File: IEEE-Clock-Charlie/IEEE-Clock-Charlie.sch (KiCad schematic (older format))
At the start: 4 parts

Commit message: First rev ordered OSHPARK
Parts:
- added L1: IEE_LOGO, IEEE-Clock-Charlie:IEEE_LOGO, symbol ADA_ROTARY:IEE_LOGO
- added R1: R, Resistor_SMD:R_0603_1608Metric, symbol Device:R
- added S1: PEC11R-4215F-S0024, IEEE-Clock-Charlie:RotaryEncoder_Alps_EC11E_Vertical_H20mm, symbol ADA_ROTARY:PEC11R-4215F-S0024
- added U4: ADA_DS3231, Connector_PinHeader_2.54mm:PinHeader_1x08_P2.54mm_Vertical, symbol ADA_DS3231:ADA_DS3231
- U1, U2, U3: renamed from U?; footprint MODULE -> IEEE-Clock-Charlie:DIP-26_1000_ELL
- gave numbers to parts that had none: 1
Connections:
- wire segments 55 -> 86
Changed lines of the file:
@@
 $EndDescr
 $Comp
-L MCU_Module:Arduino_Nano_v3.x A?
+L MCU_Module:Arduino_Nano_v3.x A1
 U 1 1 5E1FF514
 P 5550 5700
-F 0 "A?" H 5550 4611 50  0000 C CNN
+F 0 "A1" H 5550 4611 50  0000 C CNN
 F 1 "Arduino_Nano_v3.x" H 5550 4520 50  0000 C CNN
 F 2 "Module:Arduino_Nano" H 5700 4750 50  0001 L CNN
@@
 $EndComp
 $Comp
-L ADA_CHARLIE:ADA_CHARLIE U?
+L ADA_CHARLIE:ADA_CHARLIE U2
 U 1 1 5E23BD19
 P 5600 2850
-F 0 "U?" H 5600 3815 50  0000 C CNN
+F 0 "U2" H 5600 3815 50  0000 C CNN
 F 1 "ADA_CHARLIE" H 5600 3724 50  0000 C CNN
-F 2 "MODULE" H 5600 2850 50  0001 C CNN
+F 2 "IEEE-Clock-Charlie:DIP-26_1000_ELL" H 5600 2850 50  0001 C CNN
 F 3 "DOCUMENTATION" H 5600 2850 50  0001 C CNN
 	1    5600 2850
@@
 $EndComp
 $Comp
-L ADA_CHARLIE:ADA_CHARLIE U?
+L ADA_CHARLIE:ADA_CHARLIE U3
 U 1 1 5E23D5CF
 P 8400 2800
-F 0 "U?" H 8400 3765 50  0000 C CNN
+F 0 "U3" H 8400 3765 50  0000 C CNN
 F 1 "ADA_CHARLIE" H 8400 3674 50  0000 C CNN
-F 2 "MODULE" H 8400 2800 50  0001 C CNN
+F 2 "IEEE-Clock-Charlie:DIP-26_1000_ELL" H 8400 2800 50  0001 C CNN
 F 3 "DOCUMENTATION" H 8400 2800 50  0001 C CNN
 	1    8400 2800
@@
 	5750 4350 6350 4350
 $Comp
-L power:GND #PWR?
+L power:GND #PWR0101
 U 1 1 5E24D885
 P 4400 4550
-F 0 "#PWR?" H 4400 4300 50  0001 C CNN
+F 0 "#PWR0101" H 4400 4300 50  0001 C CNN
 F 1 "GND" H 4405 4377 50  0000 C CNN
 F 2 "" H 4400 4550 50  0001 C CNN
@@
 $EndComp
 $Comp
-L power:GND #PWR?
+L power:GND #PWR0102
 U 1 1 5E24E445
 P 5600 7150
-F 0 "#PWR?" H 5600 6900 50  0001 C CNN
+F 0 "#PWR0102" H 5600 6900 50  0001 C CNN
 F 1 "GND" H 5605 6977 50  0000 C CNN
 F 2 "" H 5600 7150 50  0001 C CNN
@@
 	4300 4350 5750 4350
 $Comp
-L ADA_CHARLIE:ADA_CHARLIE U?
+L ADA_CHARLIE:ADA_CHARLIE U1
 U 1 1 5E23A680
 P 3550 2800
-F 0 "U?" H 3550 3765 50  0000 C CNN
+F 0 "U1" H 3550 3765 50  0000 C CNN
 F 1 "ADA_CHARLIE" H 3550 3674 50  0000 C CNN
-F 2 "MODULE" H 3550 2800 50  0001 C CNN
+F 2 "IEEE-Clock-Charlie:DIP-26_1000_ELL" H 3550 2800 50  0001 C CNN
 F 3 "DOCUMENTATION" H 3550 2800 50  0001 C CNN
 	1    3550 2800
@@
 	2600 2300 2600 4050
 Wire Wire Line
-	2600 4050 4600 4050
+	2600 4050 3700 4050
 Connection ~ 4600 4050
+$Comp
+L ADA_DS3231:ADA_DS3231 U4
+U 1 1 5E30AA37
+P 2450 5450
+F 0 "U4" H 2292 6165 50  0000 C CNN
+F 1 "ADA_DS3231" H 2292 6074 50  0000 C CNN
+F 2 "Connector_PinHeader_2.54mm:PinHeader_1x08_P2.54mm_Vertical" H 2450 5450 50  0001 C CNN
+F 3 "DOCUMENTATION" H 2450 5450 50  0001 C CNN
+	1    2450 5450
+	-1   0    0    -1
+$EndComp
+Wire Wire Line
+	3200 5300 3600 5300
+Wire Wire Line
+	3600 5300 3600 3950
+Wire Wire Line
+	3600 3950 4500 3950
+Connection ~ 4500 3950
+Wire Wire Line
+	3200 5400 3700 5400
+Wire Wire Line
+	3700 5400 3700 4050
+Connection ~ 3700 4050
+Wire Wire Line
+	3700 4050 4600 4050
+Wire Wire Line
+	3200 5200 3300 5200
+Wire Wire Line
+	3300 5200 3300 4250
+Wire Wire Line
+	3300 4250 4400 4250
+Wire Wire Line
+	3200 5100 3200 4350
+Wire Wire Line
+	3200 4350 4300 4350
+Connection ~ 4300 4350
+Wire Wire Line
+	5050 5300 4050 5300
+Wire Wire Line
+	4050 5600 3200 5600
+$Comp
+L Device:R R1
+U 1 1 5E31C3B9
+P 4050 5450
+F 0 "R1" H 4120 5496 50  0000 L CNN
+F 1 "R" H 4120 5405 50  0000 L CNN
+F 2 "Resistor_SMD:R_0603_1608Metric" V 3980 5450 50  0001 C CNN
+F 3 "~" H 4050 5450 50  0001 C CNN
+	1    4050 5450
+	1    0    0    -1
+$EndComp
+$Comp
+L ADA_ROTARY:PEC11R-4215F-S0024 S1
+U 1 1 5E32775E
+P 3950 6250
+F 0 "S1" H 3900 6622 60  0000 C CNN
+F 1 "PEC11R-4215F-S0024" H 3900 6516 60  0000 C CNN
+F 2 "IEEE-Clock-Charlie:RotaryEncoder_Alps_EC11E_Vertical_H20mm" H 4150 6450 60  0001 L CNN
+F 3 "https://www.bourns.com/docs/Product-Datasheets/PEC11R.pdf" H 4150 6550 60  0001 L CNN
+F 4 "PEC11R-4215F-S0024-ND" H 4150 6650 60  0001 L CNN "Digi-Key_PN"
+F 5 "PEC11R-4215F-S0024" H 4150 6750 60  0001 L CNN "MPN"
+F 6 "Sensors, Transducers" H 4150 6850 60  0001 L CNN "Category"
+F 7 "Encoders" H 4150 6950 60  0001 L CNN "Family"
+F 8 "https://www.bourns.com/docs/Product-Datasheets/PEC11R.pdf" H 4150 7050 60  0001 L CNN "DK_Datasheet_Link"
+F 9 "/product-detail/en/bourns-inc/PEC11R-4215F-S0024/PEC11R-4215F-S0024-ND/4499665" H 4150 7150 60  0001 L CNN "DK_Detail_Page"
+F 10 "ROTARY ENCODER MECHANICAL 24PPR" H 4150 7250 60  0001 L CNN "Description"
+F 11 "Bourns Inc." H 4150 7350 60  0001 L CNN "Manufacturer"
+F 12 "Active" H 4150 7450 60  0001 L CNN "Status"
+	1    3950 6250
+	1    0    0    -1
+$EndComp
+Wire Wire Line
+	3250 6550 3650 6550
+Wire Wire Line
+	3650 6350 3250 6350
+Connection ~ 3250 6550
+Wire Wire Line
+	3250 6350 3250 6550
+Wire Wire Line
+	3250 6550 3250 6950
+Wire Wire Line
+	3650 6150 3250 6150
+Wire Wire Line
+	3250 6150 3250 6350
+Connection ~ 3250 6350
+Wire Wire Line
+	4150 6150 4350 6150
+Wire Wire Line
+	4350 6150 4350 5800
+Wire Wire Line
+	4350 5800 5050 5800
+Wire Wire Line
+	4150 6250 4400 6250
+Wire Wire Line
+	4400 6250 4400 5900
+Wire Wire Line
+	4400 5900 5050 5900
+Wire Wire Line
+	4150 6450 4450 6450
+Wire Wire Line
+	4450 6450 4450 6000
+Wire Wire Line
+	4450 6000 5050 6000
+$Comp
+L power:GND #PWR0103
+U 1 1 5E33C229
+P 3250 6950
+F 0 "#PWR0103" H 3250 6700 50  0001 C CNN
+F 1 "GND" H 3255 6777 50  0000 C CNN
+F 2 "" H 3250 6950 50  0001 C CNN
+F 3 "" H 3250 6950 50  0001 C CNN
+	1    3250 6950
+	1    0    0    -1
+$EndComp
+$Comp
+L ADA_ROTARY:IEE_LOGO L1
+U 1 1 5E34B000
+P 8850 5350
+F 0 "L1" H 9078 5463 50  0000 L CNN
+F 1 "IEE_LOGO" H 9078 5372 50  0000 L CNN
+F 2 "IEEE-Clock-Charlie:IEEE_LOGO" H 8850 5350 50  0001 C CNN
+F 3 "" H 8850 5350 50  0001 C CNN
+	1    8850 5350
+	1    0    0    -1
+$EndComp
+Wire Wire Line
+	8850 5500 8850 5700
+Wire Wire Line
+	6050 5650 6050 5700
+Wire Wire Line
+	6050 5700 8850 5700
 $EndSCHEMATC

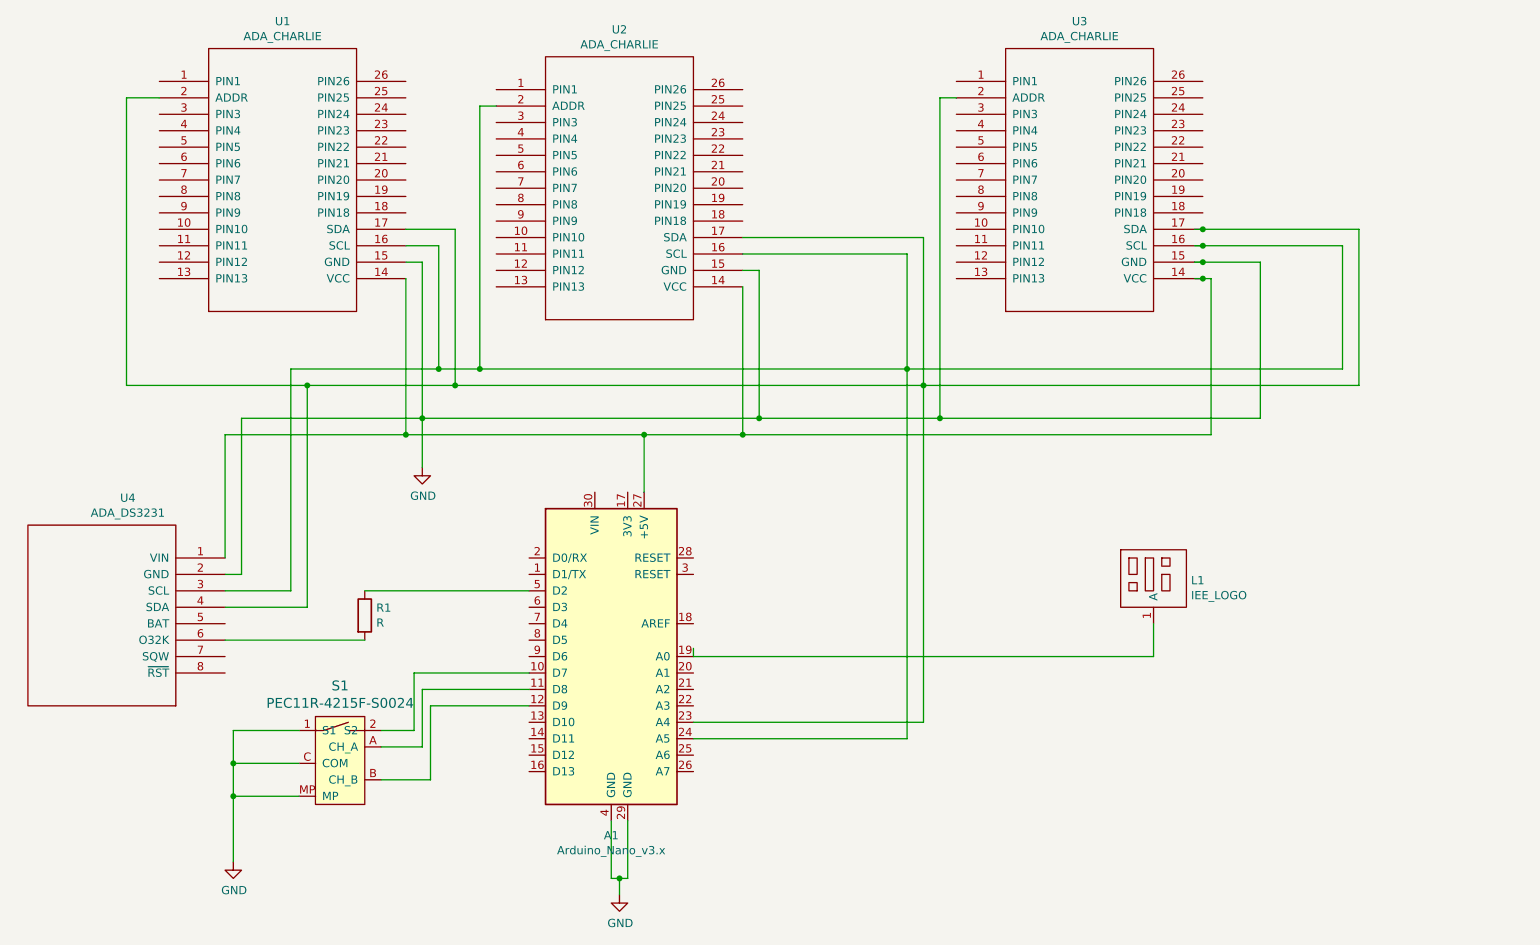
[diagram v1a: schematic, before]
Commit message: Add jumpers for CLK and DAT
Make it so displays can be individually driven rather than shared TWI
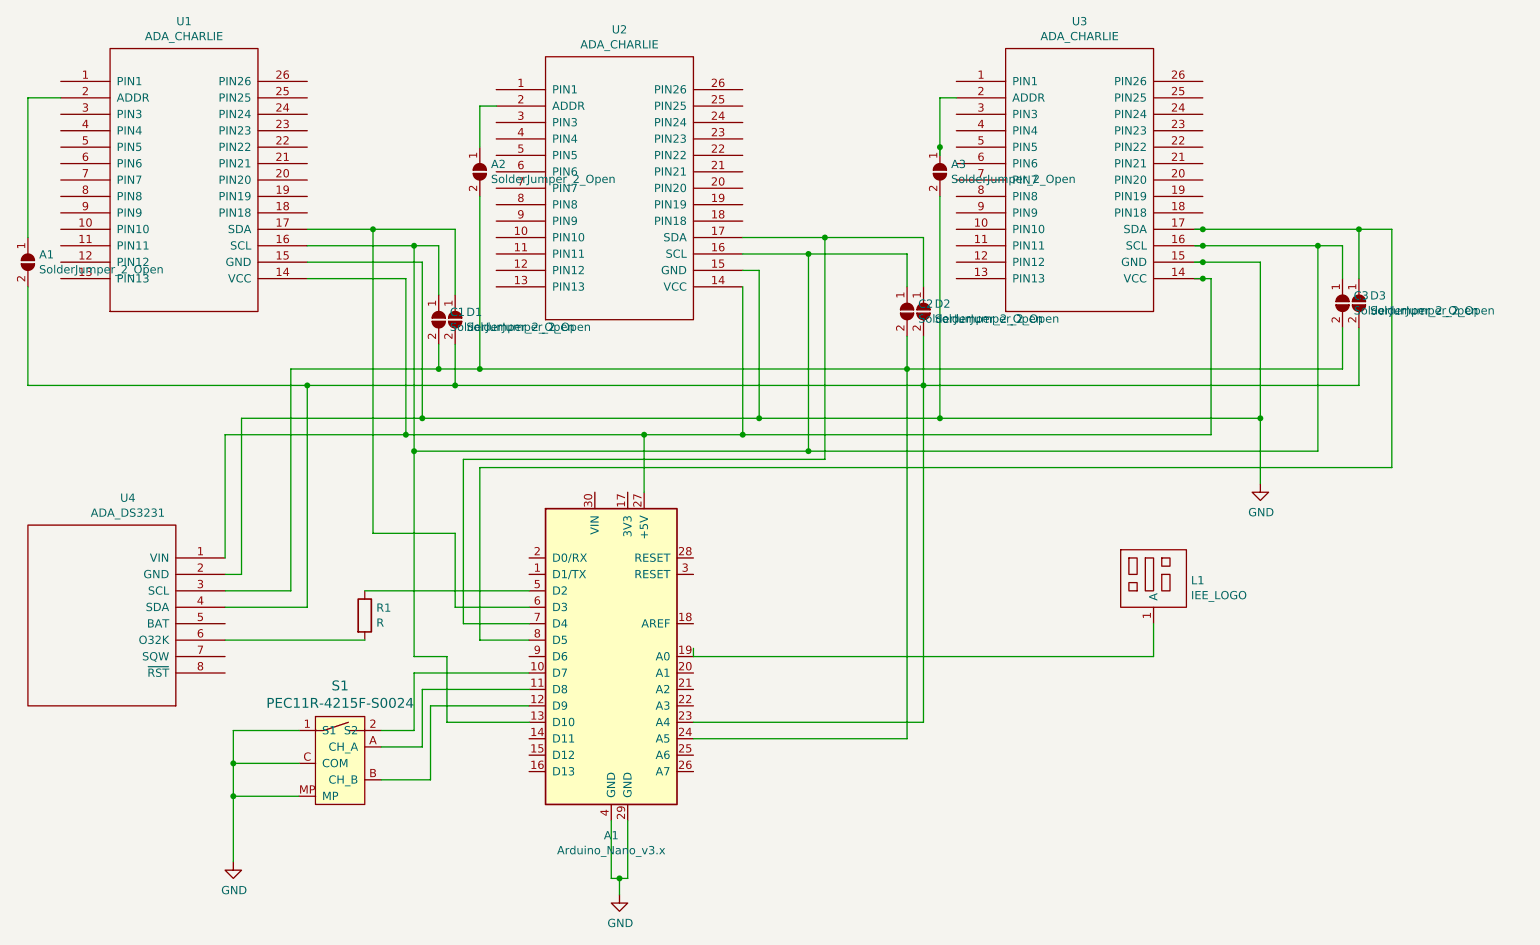
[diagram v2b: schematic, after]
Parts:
- added A1, A2, A3, C1, C2, C3, D1, D2, D3: SolderJumper_2_Open, symbol Jumper:SolderJumper_2_Open
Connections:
- wire segments 86 -> 124
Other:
- moved on the sheet: U1

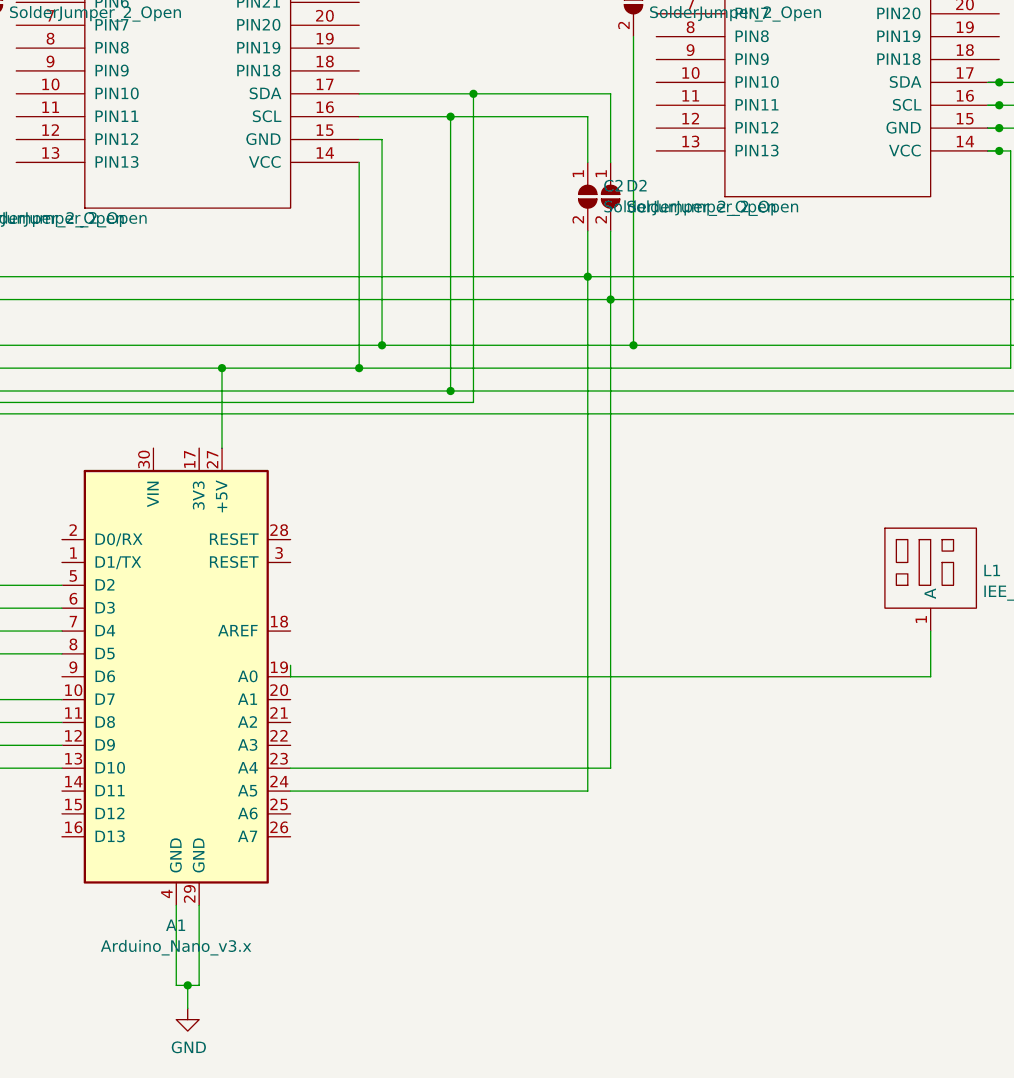
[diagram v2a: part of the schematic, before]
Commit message: With jumpers routed and ready to go
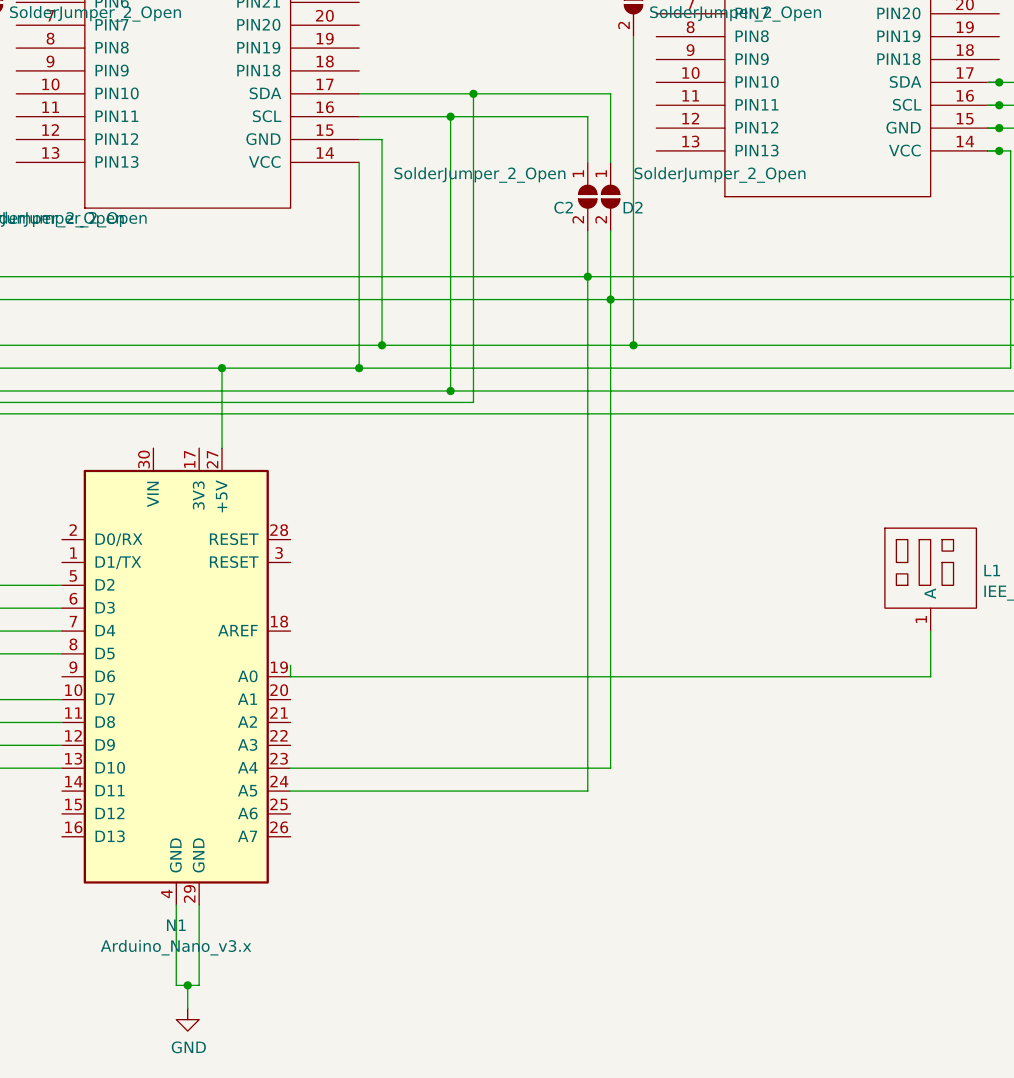
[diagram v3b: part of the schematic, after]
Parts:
- A1, A2, A3, C1, C2, C3, D1, D2, D3: footprint (none) -> Jumper:SolderJumper-2_P1.3mm_Open_RoundedPad1.0x1.5mm
- renumbered A1 to N1
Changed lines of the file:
@@
 $EndDescr
 $Comp
-L MCU_Module:Arduino_Nano_v3.x A1
+L MCU_Module:Arduino_Nano_v3.x N1
 U 1 1 5E1FF514
 P 5550 5700
-F 0 "A1" H 5550 4611 50  0000 C CNN
+F 0 "N1" H 5550 4611 50  0000 C CNN
 F 1 "Arduino_Nano_v3.x" H 5550 4520 50  0000 C CNN
 F 2 "Module:Arduino_Nano" H 5700 4750 50  0001 L CNN
@@
 F 0 "D1" V 4554 3718 50  0000 L CNN
 F 1 "SolderJumper_2_Open" V 4645 3718 50  0000 L CNN
-F 2 "" H 4600 3650 50  0001 C CNN
+F 2 "Jumper:SolderJumper-2_P1.3mm_Open_RoundedPad1.0x1.5mm" H 4600 3650 50  0001 C CNN
 F 3 "~" H 4600 3650 50  0001 C CNN
 	1    4600 3650
@@
 F 0 "C1" V 4454 3718 50  0000 L CNN
 F 1 "SolderJumper_2_Open" V 4545 3718 50  0000 L CNN
-F 2 "" H 4500 3650 50  0001 C CNN
+F 2 "Jumper:SolderJumper-2_P1.3mm_Open_RoundedPad1.0x1.5mm" H 4500 3650 50  0001 C CNN
 F 3 "~" H 4500 3650 50  0001 C CNN
 	1    4500 3650
@@
 U 1 1 5E462E54
 P 7350 3600
-F 0 "C2" V 7304 3668 50  0000 L CNN
-F 1 "SolderJumper_2_Open" V 7395 3668 50  0000 L CNN
-F 2 "" H 7350 3600 50  0001 C CNN
+F 0 "C2" V 7400 3450 50  0000 L CNN
+F 1 "SolderJumper_2_Open" V 7250 2750 50  0000 L CNN
+F 2 "Jumper:SolderJumper-2_P1.3mm_Open_RoundedPad1.0x1.5mm" H 7350 3600 50  0001 C CNN
 F 3 "~" H 7350 3600 50  0001 C CNN
 	1    7350 3600
@@
 U 1 1 5E46EEEF
 P 7450 3600
-F 0 "D2" V 7404 3668 50  0000 L CNN
-F 1 "SolderJumper_2_Open" V 7495 3668 50  0000 L CNN
-F 2 "" H 7450 3600 50  0001 C CNN
+F 0 "D2" V 7500 3650 50  0000 L CNN
+F 1 "SolderJumper_2_Open" V 7350 3700 50  0000 L CNN
+F 2 "Jumper:SolderJumper-2_P1.3mm_Open_RoundedPad1.0x1.5mm" H 7450 3600 50  0001 C CNN
 F 3 "~" H 7450 3600 50  0001 C CNN
 	1    7450 3600
@@
 F 0 "C3" V 9954 3618 50  0000 L CNN
 F 1 "SolderJumper_2_Open" V 10045 3618 50  0000 L CNN
-F 2 "" H 10000 3550 50  0001 C CNN
+F 2 "Jumper:SolderJumper-2_P1.3mm_Open_RoundedPad1.0x1.5mm" H 10000 3550 50  0001 C CNN
 F 3 "~" H 10000 3550 50  0001 C CNN
 	1    10000 3550
@@
 F 0 "D3" V 10054 3618 50  0000 L CNN
 F 1 "SolderJumper_2_Open" V 10145 3618 50  0000 L CNN
-F 2 "" H 10100 3550 50  0001 C CNN
+F 2 "Jumper:SolderJumper-2_P1.3mm_Open_RoundedPad1.0x1.5mm" H 10100 3550 50  0001 C CNN
 F 3 "~" H 10100 3550 50  0001 C CNN
 	1    10100 3550
@@
 F 0 "A3" V 7504 2818 50  0000 L CNN
 F 1 "SolderJumper_2_Open" V 7595 2818 50  0000 L CNN
-F 2 "" H 7550 2750 50  0001 C CNN
+F 2 "Jumper:SolderJumper-2_P1.3mm_Open_RoundedPad1.0x1.5mm" H 7550 2750 50  0001 C CNN
 F 3 "~" H 7550 2750 50  0001 C CNN
 	1    7550 2750
@@
 F 0 "A2" V 4704 2818 50  0000 L CNN
 F 1 "SolderJumper_2_Open" V 4795 2818 50  0000 L CNN
-F 2 "" H 4750 2750 50  0001 C CNN
+F 2 "Jumper:SolderJumper-2_P1.3mm_Open_RoundedPad1.0x1.5mm" H 4750 2750 50  0001 C CNN
 F 3 "~" H 4750 2750 50  0001 C CNN
 	1    4750 2750
@@
 F 0 "A1" V 1954 3368 50  0000 L CNN
 F 1 "SolderJumper_2_Open" V 2045 3368 50  0000 L CNN
-F 2 "" H 2000 3300 50  0001 C CNN
+F 2 "Jumper:SolderJumper-2_P1.3mm_Open_RoundedPad1.0x1.5mm" H 2000 3300 50  0001 C CNN
 F 3 "~" H 2000 3300 50  0001 C CNN
 	1    2000 3300
